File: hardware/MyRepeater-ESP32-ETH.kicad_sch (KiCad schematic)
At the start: 28 parts, among them J1 UART, J2 230V AC, Q1 BC547, Q2 BC547, SW1 RESET, U1 ESP32-WROOM-32, U2 LAN8720 Module, U3 NRF24L01+ PA-LNA, U4 DS18B20, U5 mini_esp32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

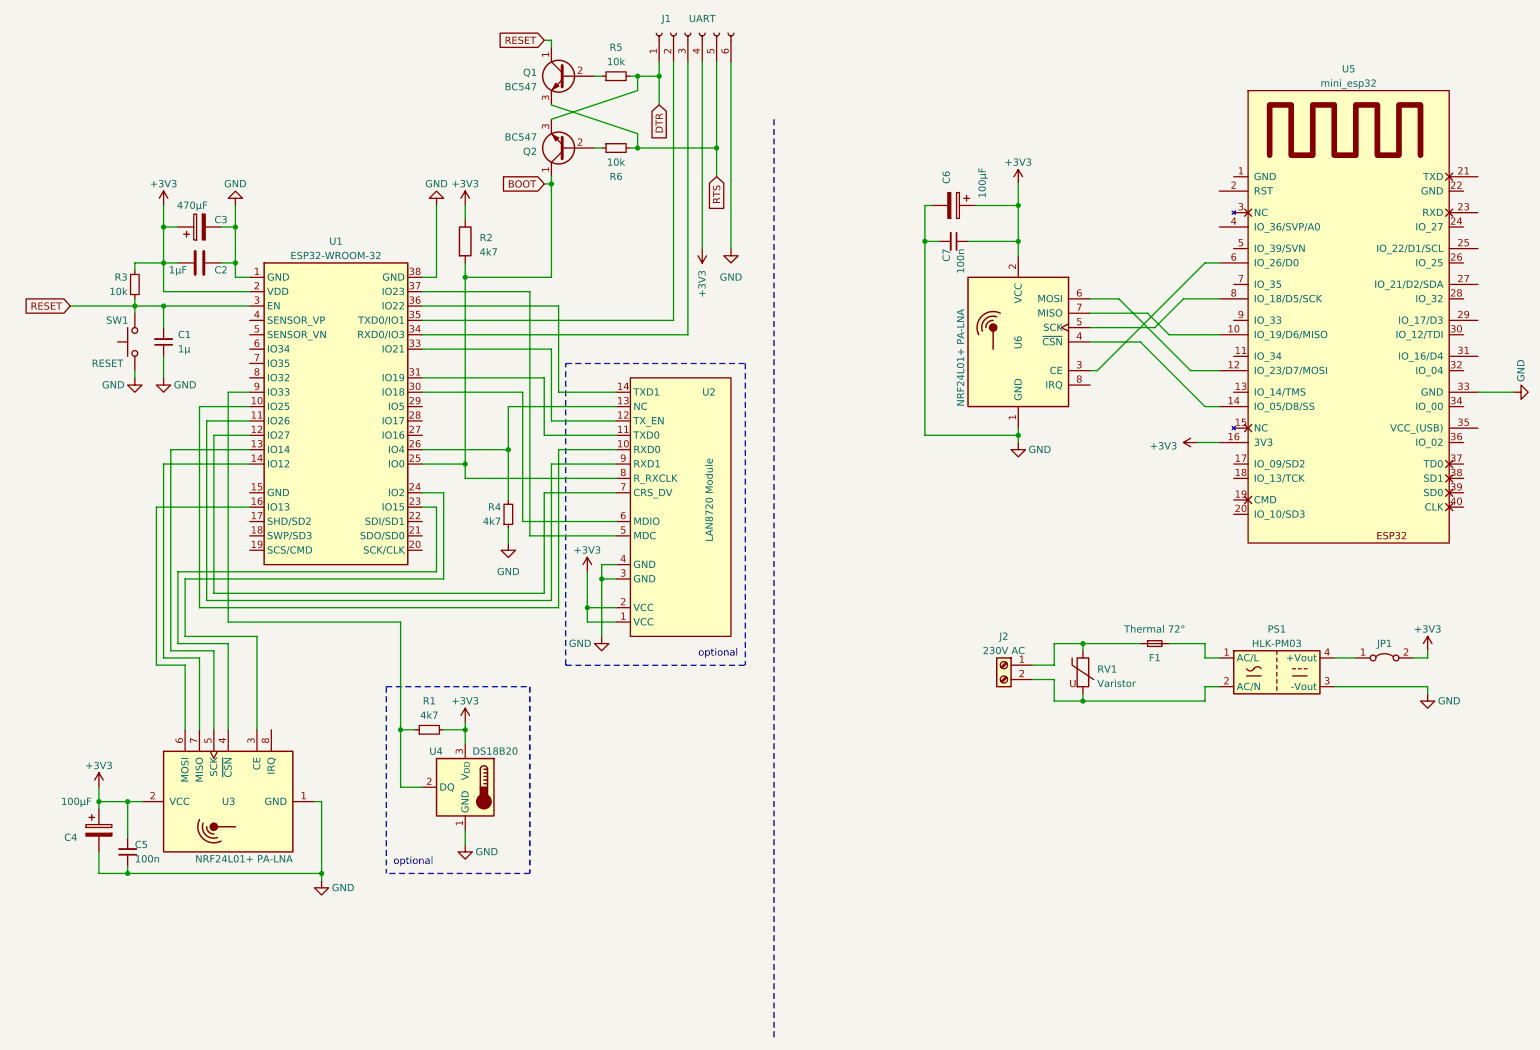
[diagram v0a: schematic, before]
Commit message: updated schematic and BOM
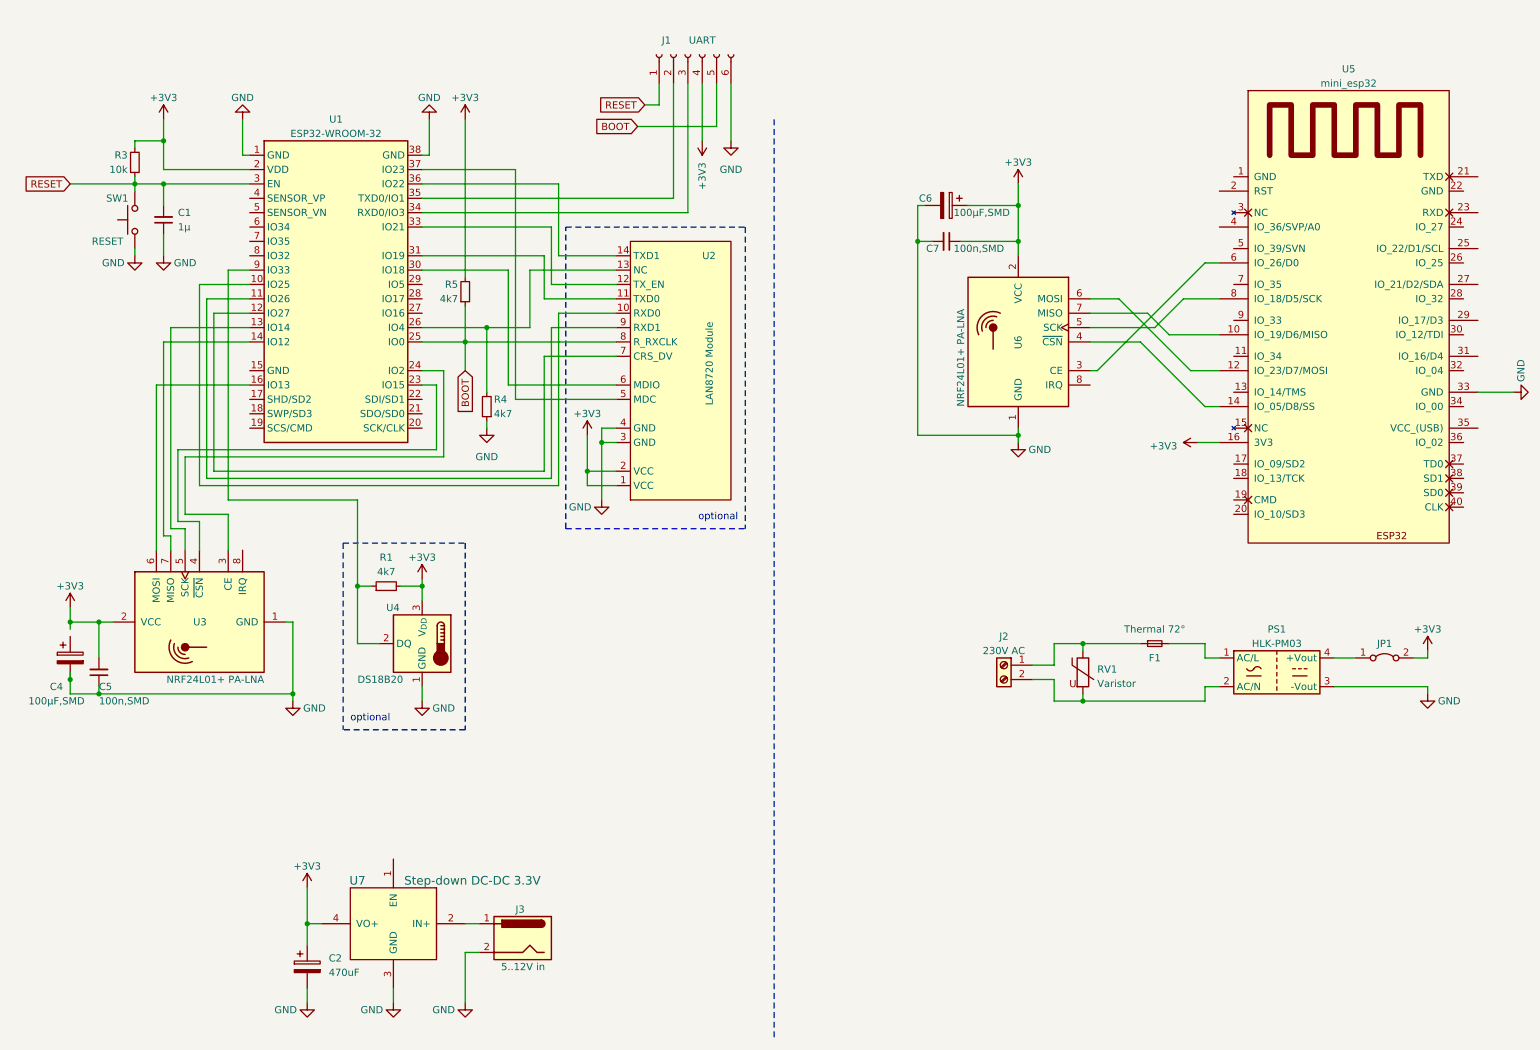
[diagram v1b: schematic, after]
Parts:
- removed C2: 1µF, symbol Device:C
- removed C3: 470µF, symbol Device:C_Polarized
- removed Q1, Q2: BC547, Package_TO_SOT_THT:TO-92_Inline, symbol Transistor_BJT:BC547
- removed R2: 4k7, symbol Device:R
- removed R6: 10k, symbol Device:R_Small
- added C2: 470uF, symbol Device:C_Polarized
- added J3: 5..12V in, symbol Connector:Barrel_Jack
- added U7: Step-down DC-DC 3.3V, symbol eBay:DC_DC_fix
- C4, C6: value 100µF -> 100µF,SMD
- C5, C7: value 100n -> 100n,SMD
- R5: value 10k -> 4k7
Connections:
- net RTS is gone; now on net BOOT: J1.5 (Pin_5)
- net +3V3: now also R5.2, C2.1, U7.4 (VO+); no longer C4.1
- net BOOT: now also R5.1
- net GND: now also C2.2, J3.2, U7.3 (GND)
- net RESET: now also J1.1 (Pin_1)
- removed net DTR: J1.1 (Pin_1), R5.2
- new net: J3.1, U7.2 (IN+)
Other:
- moved on the sheet: C1, C4, C5, C6, C7, J1, R1, R3, R4, SW1, U1, U2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
